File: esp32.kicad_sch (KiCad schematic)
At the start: 40 parts, among them J1 USB_C, J14 PWR_CONN, J15 SPI_0, J16 SPI_1, J17 SPI_2, J2 USB_C_UART, J3 A0, J4 A1, J5 A2, J6 D0, J7 D1, Q1 S8050, Q2 S8050, SW1 SW_RST, SW2 SW_BOOT, U3 ESP32-S3-WROOM-1, U4 CH340C

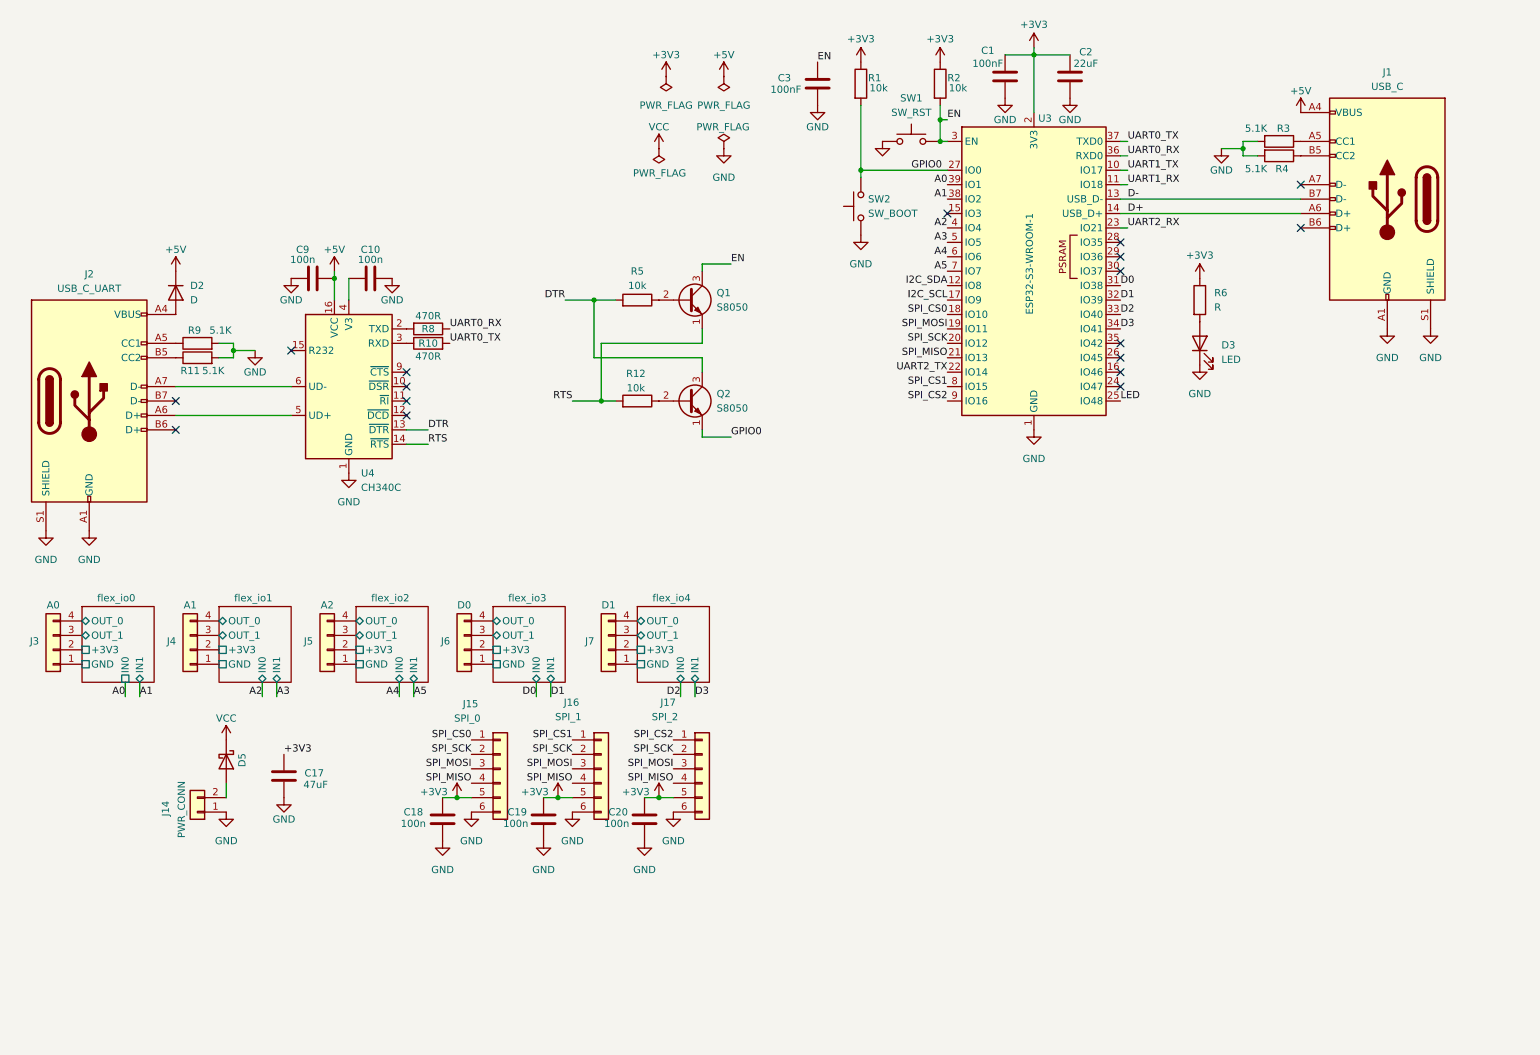
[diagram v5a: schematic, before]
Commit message: rest components placed
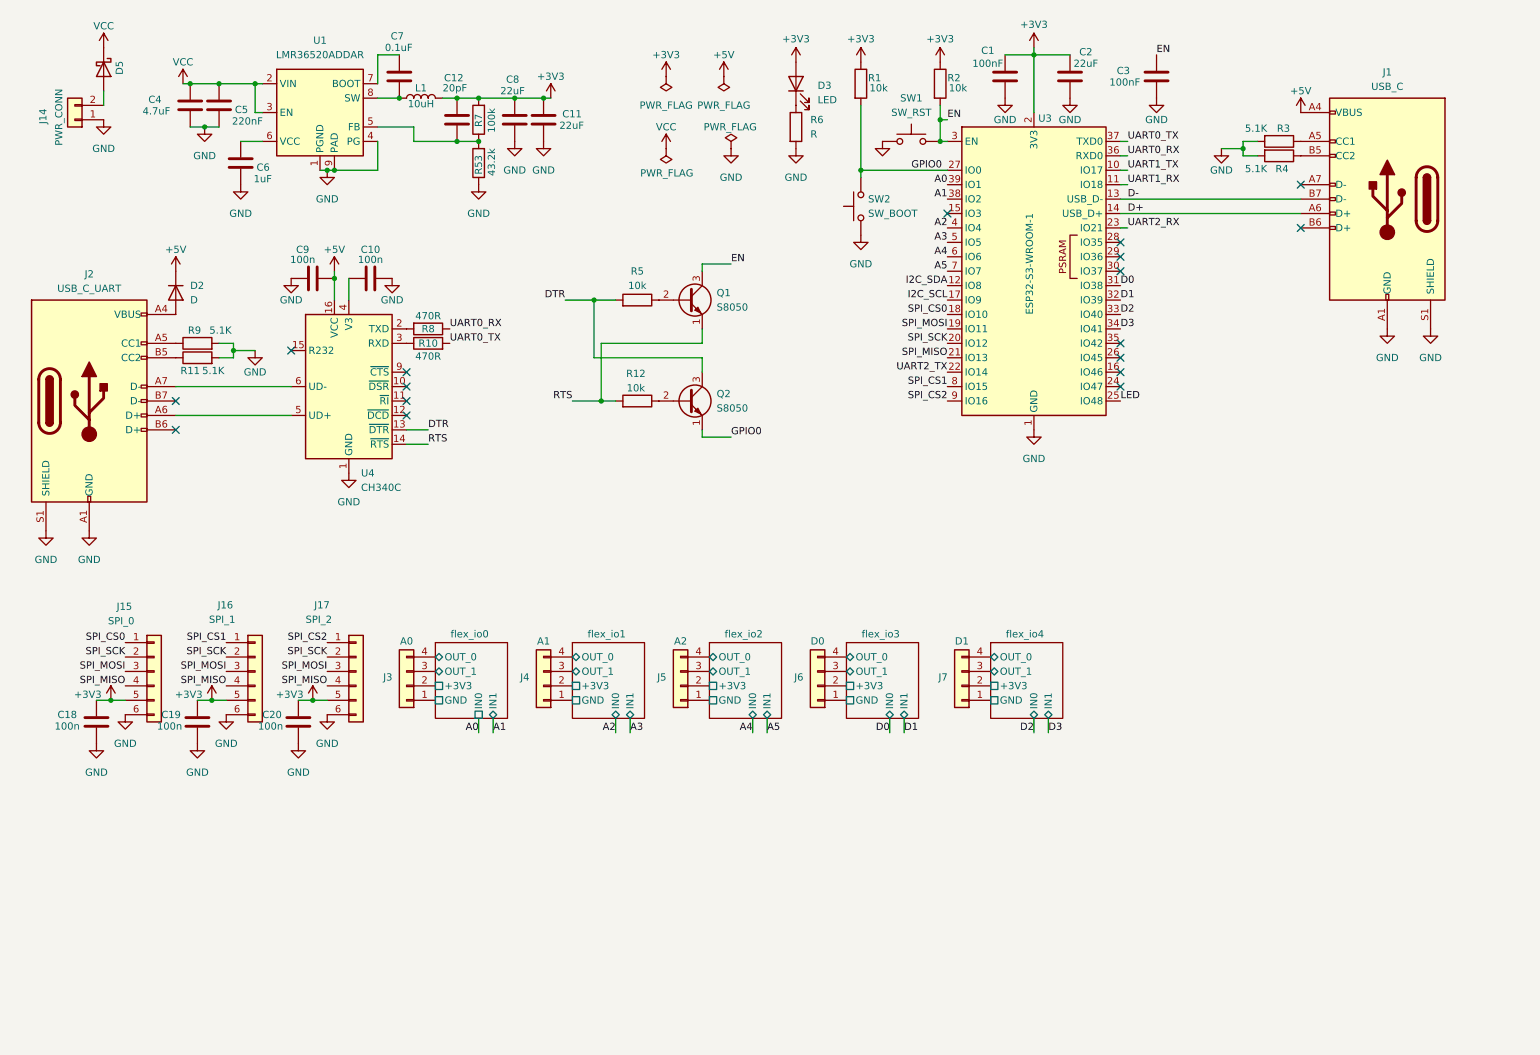
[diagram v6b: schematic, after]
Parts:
- removed C17: 47uF, Capacitor_THT:C_Radial_D6.3mm_H5.0mm_P2.50mm, symbol Device:C
- added C11, C8: 22uF, Capacitor_SMD:C_0805_2012Metric_Pad1.18x1.45mm_HandSolder, symbol Device:C
- added C12: 20pF, Capacitor_SMD:C_0805_2012Metric_Pad1.18x1.45mm_HandSolder, symbol Device:C
- added C4: 4.7uF, Capacitor_SMD:C_0805_2012Metric_Pad1.18x1.45mm_HandSolder, symbol Device:C
- added C5: 220nF, Capacitor_SMD:C_0805_2012Metric_Pad1.18x1.45mm_HandSolder, symbol Device:C
- added C6: 1uF, Capacitor_SMD:C_0805_2012Metric_Pad1.18x1.45mm_HandSolder, symbol Device:C
- added C7: 0.1uF, Capacitor_SMD:C_0805_2012Metric_Pad1.18x1.45mm_HandSolder, symbol Device:C
- added L1: 10uH, Inductor_SMD:L_Chilisin_BMRA00050530, symbol Device:L
- added R53: 43.2k, Resistor_SMD:R_0805_2012Metric_Pad1.20x1.40mm_HandSolder, symbol Device:R
- added R7: 100k, Resistor_SMD:R_0805_2012Metric_Pad1.20x1.40mm_HandSolder, symbol Device:R
- added U1: LMR36520ADDAR, Package_SO:Texas_HTSOP-8-1EP_3.9x4.9mm_P1.27mm_EP2.95x4.9mm_Mask2.4x3.1mm_ThermalVias, symbol Regulator_Switching:LMR36510ADDA
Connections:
- net +3V3: now also D3.2 (A), C11.1, C12.1, C8.1, L1.2, R7.2; no longer R6.1
- net GND: now also R6.2, C11.2, C4.2, C5.2, C6.2, C8.2, R53.1, U1.1 (PGND), U1.4 (PG), U1.9 (PAD); no longer D3.1 (K)
- net VCC: now also C4.1, C5.1, U1.2 (VIN), U1.3 (EN)
- new net: D3.1 (K), R6.1
- new net: C12.2, R53.2, R7.1, U1.5 (FB)
- new net: C6.1, U1.6 (VCC)
- new net: C7.1, U1.7 (BOOT)
- new net: C7.2, L1.1, U1.8 (SW)
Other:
- moved on the sheet: C18, C19, C20, C3, D3, D5, J14, J15, J16, J17, J3, J4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

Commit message: without uart converter, small version
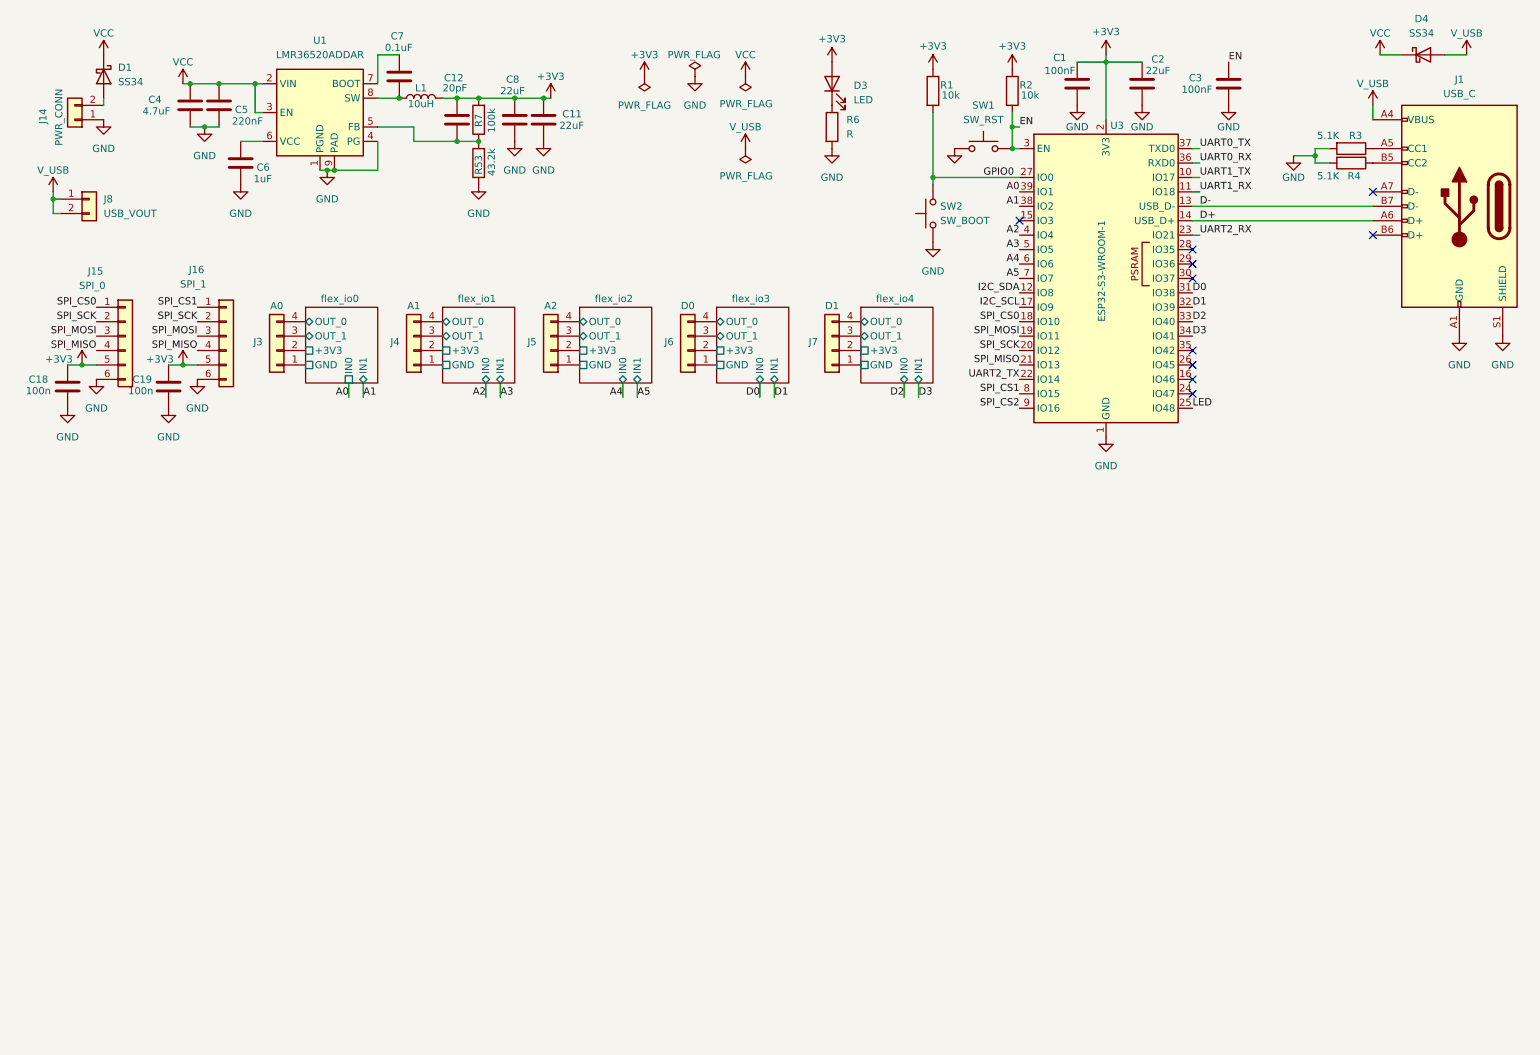
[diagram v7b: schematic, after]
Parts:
- removed C10, C20, C9: 100n, Capacitor_SMD:C_0805_2012Metric_Pad1.18x1.45mm_HandSolder, symbol Device:C
- removed D2: D, Diode_SMD:D_0805_2012Metric_Pad1.15x1.40mm_HandSolder, symbol Device:D
- removed D5: SS34, Diode_SMD:D_SMA-SMB_Universal_Handsoldering, symbol Device:D_Schottky
- removed J17: SPI_2, Connector_JST:JST_PH_B6B-PH-K_1x06_P2.00mm_Vertical, symbol Connector_Generic:Conn_01x06
- removed J2: USB_C_UART, Connector_USB:USB_C_Receptacle_HRO_TYPE-C-31-M-12, symbol Connector:USB_C_Receptacle_USB2.0_14P
- removed Q1, Q2: S8050, Package_TO_SOT_SMD:TSOT-23_HandSoldering, symbol Transistor_BJT:S8050
- removed R10, R8: 470R, Resistor_SMD:R_0805_2012Metric_Pad1.20x1.40mm_HandSolder, symbol Device:R
- removed R11, R9: 5.1K, Resistor_SMD:R_0805_2012Metric_Pad1.20x1.40mm_HandSolder, symbol Device:R
- removed R12, R5: 10k, Resistor_SMD:R_0805_2012Metric_Pad1.20x1.40mm_HandSolder, symbol Device:R
- removed U4: CH340C, Package_SO:SOIC-16_3.9x9.9mm_P1.27mm, symbol Interface_USB:CH340C
- added D1, D4: SS34, Diode_SMD:D_SMA, symbol Diode:SS34
- added J8: USB_VOUT, Connector_PinHeader_2.54mm:PinHeader_2x01_P2.54mm_Vertical, symbol Connector_Generic:Conn_01x02
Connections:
- net VCC: now also D1.1 (K), D4.1 (K)
- net at J14.2 (Pin_2): now also D1.2 (A)
- net +5V renamed V_USB
- net V_USB: now also D4.2 (A), J8.1 (Pin_1), J8.2 (Pin_2)
- no-connect marks 17 -> 10
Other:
- moved on the sheet: C1, C18, C19, C2, C3, D3, J1, J15, J16, J3, J4, J5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

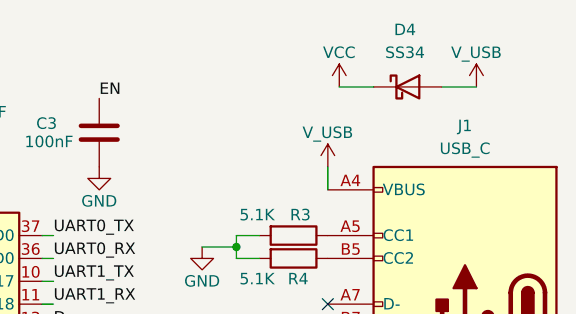
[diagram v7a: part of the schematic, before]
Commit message: change footprints for better soldering
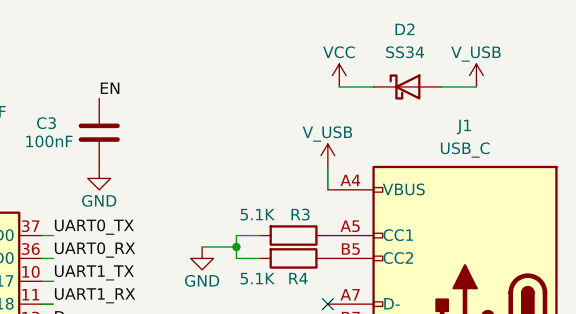
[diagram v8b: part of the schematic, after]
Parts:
- removed D4: SS34, Diode_SMD:D_SMA, symbol Diode:SS34
- added D2: SS34, Diode_SMD:D_SMB_Handsoldering, symbol Diode:SS34
- C4, C5: footprint Capacitor_SMD:C_0805_2012Metric_Pad1.18x1.45mm_HandSolder -> Library:C_1206&0805
- D1: footprint Diode_SMD:D_SMA -> Diode_SMD:D_SMB_Handsoldering
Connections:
- net VCC: now also D2.1 (K)
- net V_USB: now also D2.2 (A)
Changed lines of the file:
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@@
 			)
 		)
-		(property "Footprint" "Diode_SMD:D_SMA"
+		(property "Footprint" "Diode_SMD:D_SMB_Handsoldering"
 			(at 26.035 26.67 0)
 			(effects
@@
 			)
 		)
-		(property "Footprint" "Capacitor_SMD:C_0805_2012Metric_Pad1.18x1.45mm_HandSolder"
+		(property "Footprint" "Library:C_1206&0805"
 			(at 46.6852 35.56 0)
 			(effects
@@
 	)
 	(symbol
-		(lib_id "Diode:SS34")
-		(at 262.89 22.86 0)
-		(unit 1)
-		(exclude_from_sim no)
-		(in_bom yes)
-		(on_board yes)
-		(dnp no)
-		(fields_autoplaced yes)
-		(property "Reference" "D4"
-			(at 262.5725 16.51 0)
-			(effects
-				(font
-					(size 1.27 1.27)
-				)
-			)
-		)
-		(property "Value" "SS34"
-			(at 262.5725 19.05 0)
-			(effects
-				(font
-					(size 1.27 1.27)
-				)
-			)
-		)
-		(property "Footprint" "Diode_SMD:D_SMA"
-			(at 262.89 27.305 0)
-			(effects
-				(font
-					(size 1.27 1.27)
-				)
-				(hide yes)
-			)
-		)
-		(property "Datasheet" "https://www.vishay.com/docs/88751/ss32.pdf"
-			(at 262.89 22.86 0)
-			(effects
-				(font
-					(size 1.27 1.27)
-				)
-				(hide yes)
-			)
-		)
-		(property "Description" "40V 3A Schottky Diode, SMA"
-			(at 262.89 22.86 0)
-			(effects
-				(font
-					(size 1.27 1.27)
-				)
-				(hide yes)
-			)
-		)
-		(pin "2"
-		)
-		(pin "1"
-		)
-		(instances
-			(project "esp32"
-				(path "/ea80ac25-815d-4e11-85a3-2f7286372b15"
-					(reference "D4")
-					(unit 1)
-				)
-			)
-		)
-	)
-	(symbol
 		(lib_id "Device:C")
 		(at 213.36 27.94 180)
@@
 			)
 		)
-		(property "Footprint" "Capacitor_SMD:C_0805_2012Metric_Pad1.18x1.45mm_HandSolder"
+		(property "Footprint" "Library:C_1206&0805"
 			(at 51.7652 35.56 0)
 			(effects
@@
 					(unit 1)
 				)
+			)
+		)
+	)
+	(symbol
+		(lib_id "Diode:SS34")
+		(at 262.89 22.86 0)
+		(unit 1)
+		(exclude_from_sim no)
+		(in_bom yes)
+		(on_board yes)
+		(dnp no)
+		(fields_autoplaced yes)
+		(property "Reference" "D2"
+			(at 262.5725 16.51 0)
+			(effects
+				(font
+					(size 1.27 1.27)
+				)
+			)
+		)
+		(property "Value" "SS34"
+			(at 262.5725 19.05 0)
+			(effects
+				(font
+					(size 1.27 1.27)
+				)
+			)
+		)
+		(property "Footprint" "Diode_SMD:D_SMB_Handsoldering"
+			(at 262.89 27.305 0)
+			(effects
+				(font
+					(size 1.27 1.27)
+				)
+				(hide yes)
+			)
+		)
+		(property "Datasheet" "https://www.vishay.com/docs/88751/ss32.pdf"
+			(at 262.89 22.86 0)
+			(effects
+				(font
+					(size 1.27 1.27)
+				)
+				(hide yes)
+			)
+		)
+		(property "Description" "40V 3A Schottky Diode, SMA"
+			(at 262.89 22.86 0)
+			(effects
+				(font
+					(size 1.27 1.27)
+				)
+				(hide yes)
+			)
+		)
+		(pin "2"
+		)
+		(pin "1"
+		)
+		(instances
+			(project "esp32"
+				(path "/ea80ac25-815d-4e11-85a3-2f7286372b15"
+					(reference "D2")
+					(unit 1)
+				)
